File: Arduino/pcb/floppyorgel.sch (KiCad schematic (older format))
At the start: 2 parts, among them J1 VCC_Power_Select

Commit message: pcb: add switch for VCC power select
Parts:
- J1: footprint Connector_PinHeader_2.54mm:PinHeader_1x03_P2.54mm_Vertical -> w_switch:switch_mmp122-r
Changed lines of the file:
@@
 F 0 "J1" H 5672 2357 50  0000 R CNN
 F 1 "VCC_Power_Select" H 5672 2448 50  0000 R CNN
-F 2 "Connector_PinHeader_2.54mm:PinHeader_1x03_P2.54mm_Vertical" H 5700 2425 50  0001 C CNN
+F 2 "w_switch:switch_mmp122-r" H 5700 2425 50  0001 C CNN
 F 3 "~" H 5700 2425 50  0001 C CNN
 	1    5700 2425

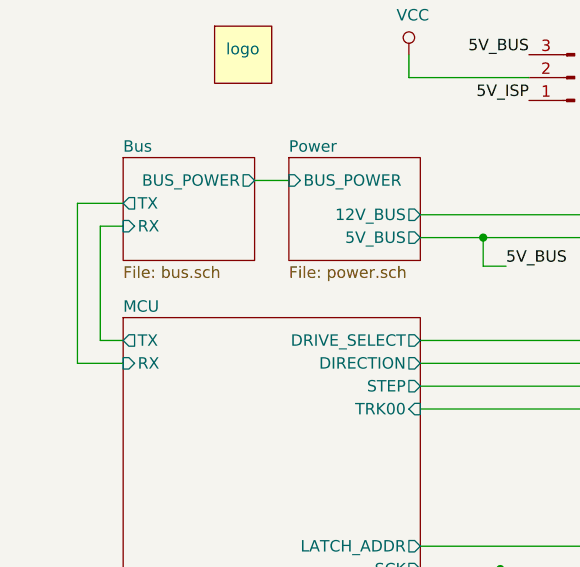
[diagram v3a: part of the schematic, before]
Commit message: pcb: mcu / bus: improve TX/RX labels for RS485 transceiver
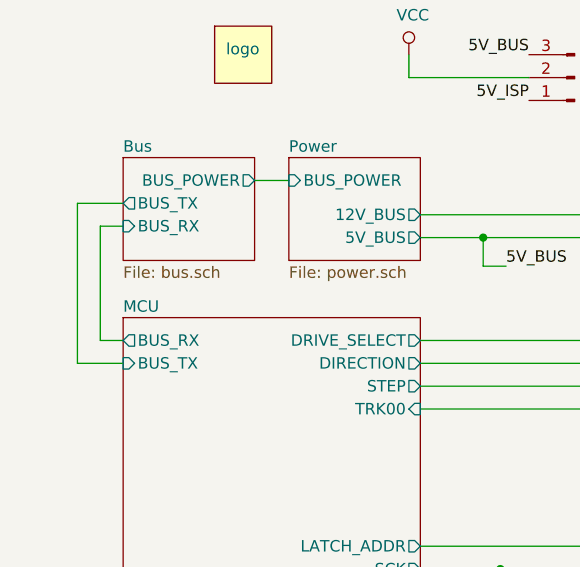
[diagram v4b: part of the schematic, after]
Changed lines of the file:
@@
 F1 "bus.sch" 50
 F2 "BUS_POWER" O R 4300 2875 50
-F3 "TX" O L 3725 2975 50
-F4 "RX" I L 3725 3075 50
+F3 "BUS_TX" O L 3725 2975 50
+F4 "BUS_RX" I L 3725 3075 50
 $EndSheet
 $Sheet
@@
 F10 "MISO" O L 5800 4675 50
 $EndSheet
-$Sheet
-S 3725 3475 1300 1950
-U 5CCFEC3E
-F0 "MCU" 50
-F1 "mcu.sch" 50
-F2 "DRIVE_SELECT" O R 5025 3575 50
-F3 "DIRECTION" O R 5025 3675 50
-F4 "STEP" O R 5025 3775 50
-F5 "MISO" I R 5025 4675 50
-F6 "SCK" O R 5025 4575 50
-F7 "TRK00" I R 5025 3875 50
-F8 "LATCH_ADDR" O R 5025 4475 50
-F9 "5V_ISP" O L 3725 5250 50
-F10 "RX" I L 3725 3675 50
-F11 "TX" O L 3725 3575 50
-F12 "LATCH_LED" O R 5025 5125 50
-F13 "MOSI" O R 5025 5225 50
-$EndSheet
 Text Label 5500 2325 2    50   ~ 0
 5V_BUS
@@
 	1    0    0    -1
 $EndComp
+$Sheet
+S 3725 3475 1300 1950
+U 5CCFEC3E
+F0 "MCU" 50
+F1 "mcu.sch" 50
+F2 "DRIVE_SELECT" O R 5025 3575 50
+F3 "DIRECTION" O R 5025 3675 50
+F4 "STEP" O R 5025 3775 50
+F5 "MISO" I R 5025 4675 50
+F6 "SCK" O R 5025 4575 50
+F7 "TRK00" I R 5025 3875 50
+F8 "LATCH_ADDR" O R 5025 4475 50
+F9 "5V_ISP" O L 3725 5250 50
+F10 "LATCH_LED" O R 5025 5125 50
+F11 "MOSI" O R 5025 5225 50
+F12 "BUS_TX" I L 3725 3675 50
+F13 "BUS_RX" O L 3725 3575 50
+$EndSheet
 $EndSCHEMATC

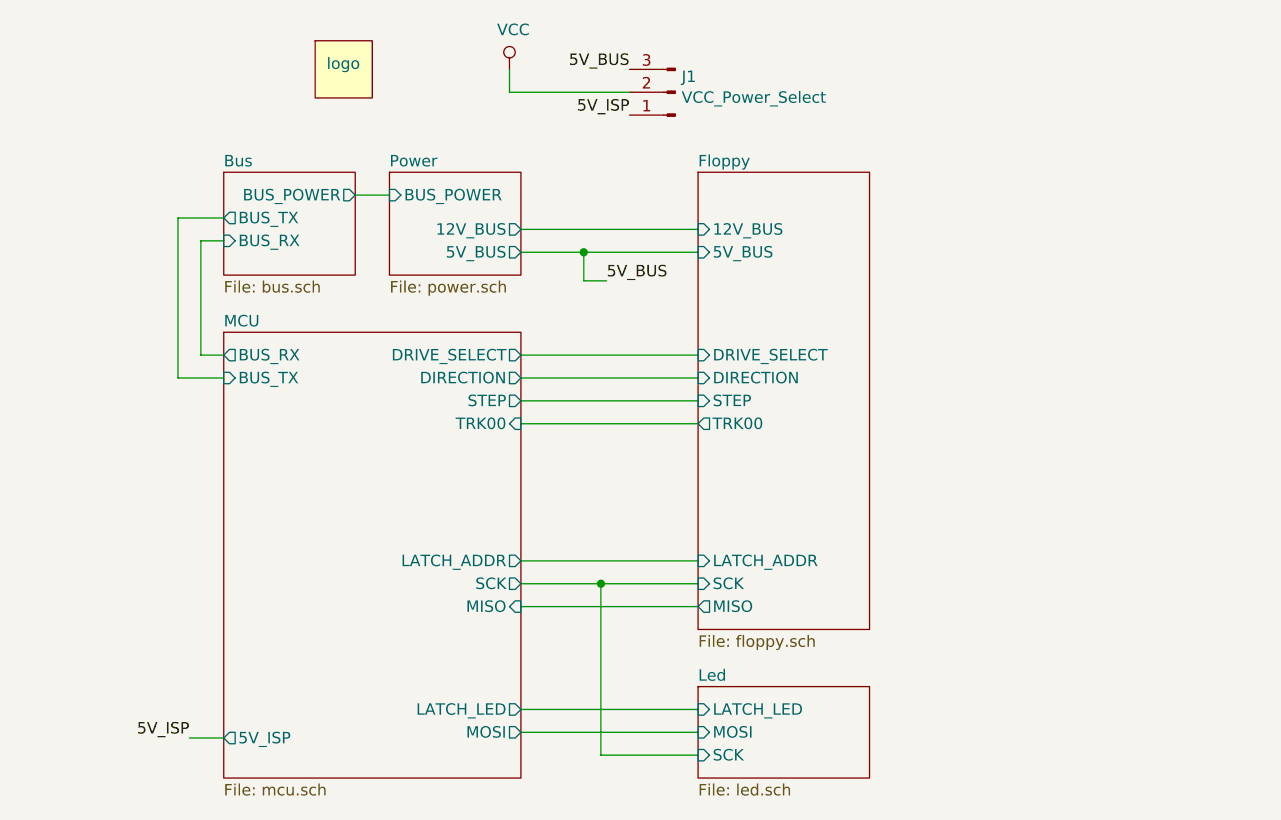
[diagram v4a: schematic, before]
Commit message: pcb / floppy: remove 4094 shift register / connect address connector directly
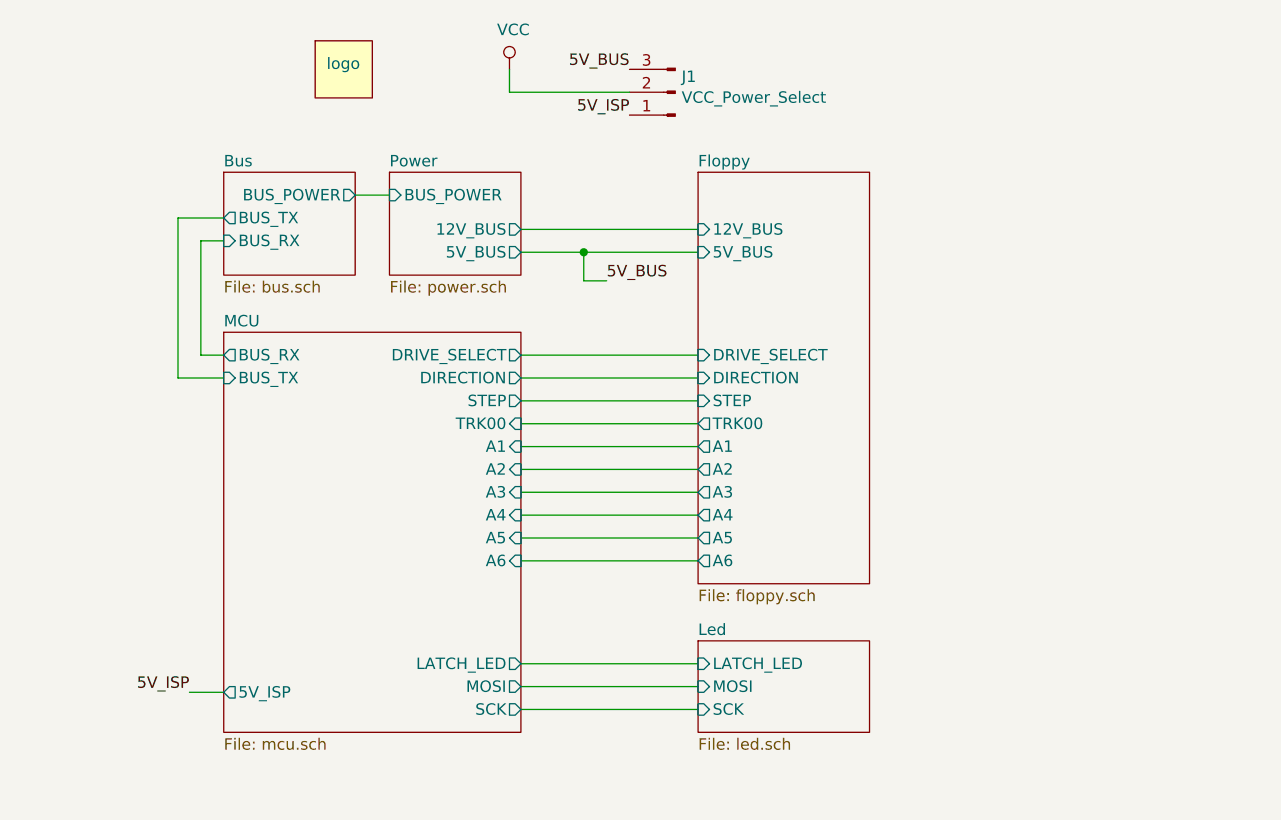
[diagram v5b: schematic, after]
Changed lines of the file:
@@
 Wire Wire Line
 	5800 3775 5025 3775
-$Comp
-L power:VCC #PWR01
-U 1 1 5D10B089
-P 4975 2325
-AR Path="/5D10B089" Ref="#PWR01"  Part="1"
-AR Path="/5CD31258/5D10B089" Ref="#PWR?"  Part="1"
-F 0 "#PWR01" H 4975 2175 50  0001 C CNN
-F 1 "VCC" H 4992 2498 50  0000 C CNN
-F 2 "" H 4975 2325 50  0001 C CNN
-F 3 "" H 4975 2325 50  0001 C CNN
-	1    4975 2325
-	1    0    0    -1
-$EndComp
-Wire Wire Line
-	4975 2325 4975 2425
-Wire Wire Line
-	4975 2425 5500 2425
-$Comp
-L vcc_power_select:VCC_Power_Select J1
-U 1 1 5D19C0BF
-P 5700 2425
-F 0 "J1" H 5672 2357 50  0000 R CNN
-F 1 "VCC_Power_Select" H 5672 2448 50  0000 R CNN
-F 2 "w_switch:switch_mmp122-r" H 5700 2425 50  0001 C CNN
-F 3 "~" H 5700 2425 50  0001 C CNN
-	1    5700 2425
-	-1   0    0    1
-$EndComp
-Wire Wire Line
-	5800 4675 5025 4675
-Wire Wire Line
-	5025 4475 5800 4475
 Wire Wire Line
 	3625 3575 3725 3575
@@
 Wire Wire Line
 	5025 3025 5800 3025
-Text Label 5500 2525 2    50   ~ 0
-5V_ISP
-Wire Wire Line
-	3575 5250 3725 5250
-Text Label 3575 5250 2    50   ~ 0
-5V_ISP
 Wire Wire Line
 	5025 3575 5800 3575
 Wire Wire Line
 	5025 3675 5800 3675
-$Sheet
-S 5800 2775 750  2000
-U 5CD0EE48
-F0 "Floppy" 50
-F1 "floppy.sch" 50
-F2 "DRIVE_SELECT" I L 5800 3575 50
-F3 "DIRECTION" I L 5800 3675 50
-F4 "TRK00" O L 5800 3875 50
-F5 "STEP" I L 5800 3775 50
-F6 "5V_BUS" I L 5800 3125 50
-F7 "12V_BUS" I L 5800 3025 50
-F8 "LATCH_ADDR" I L 5800 4475 50
-F9 "SCK" I L 5800 4575 50
-F10 "MISO" O L 5800 4675 50
-$EndSheet
-Text Label 5500 2325 2    50   ~ 0
-5V_BUS
 Wire Wire Line
 	5025 3125 5300 3125
@@
 	5300 3125 5800 3125
 $Sheet
-S 5800 5025 750  400
+S 5800 4825 750  400
 U 5CD3FBA6
 F0 "Led" 50
 F1 "led.sch" 50
-F2 "MOSI" I L 5800 5225 50
-F3 "SCK" I L 5800 5325 50
-F4 "LATCH_LED" I L 5800 5125 50
+F2 "MOSI" I L 5800 5025 50
+F3 "SCK" I L 5800 5125 50
+F4 "LATCH_LED" I L 5800 4925 50
 $EndSheet
 Wire Wire Line
-	5025 4575 5375 4575
+	5025 4275 5800 4275
 Wire Wire Line
-	5025 5125 5800 5125
-Connection ~ 5375 4575
+	5025 4375 5800 4375
 Wire Wire Line
-	5375 4575 5800 4575
+	5025 4475 5800 4475
 Wire Wire Line
-	5800 5325 5375 5325
+	5025 4175 5800 4175
 Wire Wire Line
-	5375 4575 5375 5325
+	5800 4075 5025 4075
 Wire Wire Line
-	5025 5225 5800 5225
+	5025 3975 5800 3975
 $Comp
 L logo:logo L1
@@
 	1    0    0    -1
 $EndComp
+Text Label 5500 2325 2    50   ~ 0
+5V_BUS
+Text Label 5500 2525 2    50   ~ 0
+5V_ISP
+$Comp
+L vcc_power_select:VCC_Power_Select J1
+U 1 1 5D19C0BF
+P 5700 2425
+F 0 "J1" H 5672 2357 50  0000 R CNN
+F 1 "VCC_Power_Select" H 5672 2448 50  0000 R CNN
+F 2 "w_switch:switch_mmp122-r" H 5700 2425 50  0001 C CNN
+F 3 "~" H 5700 2425 50  0001 C CNN
+	1    5700 2425
+	-1   0    0    1
+$EndComp
+Wire Wire Line
+	4975 2425 5500 2425
+Wire Wire Line
+	4975 2325 4975 2425
+$Comp
+L power:VCC #PWR01
+U 1 1 5D10B089
+P 4975 2325
+AR Path="/5D10B089" Ref="#PWR01"  Part="1"
+AR Path="/5CD31258/5D10B089" Ref="#PWR?"  Part="1"
+F 0 "#PWR01" H 4975 2175 50  0001 C CNN
+F 1 "VCC" H 4992 2498 50  0000 C CNN
+F 2 "" H 4975 2325 50  0001 C CNN
+F 3 "" H 4975 2325 50  0001 C CNN
+	1    4975 2325
+	1    0    0    -1
+$EndComp
 $Sheet
-S 3725 3475 1300 1950
+S 5800 2775 750  1800
+U 5CD0EE48
+F0 "Floppy" 50
+F1 "floppy.sch" 50
+F2 "DRIVE_SELECT" I L 5800 3575 50
+F3 "DIRECTION" I L 5800 3675 50
+F4 "TRK00" O L 5800 3875 50
+F5 "STEP" I L 5800 3775 50
+F6 "5V_BUS" I L 5800 3125 50
+F7 "12V_BUS" I L 5800 3025 50
+F8 "A4" O L 5800 4275 50
+F9 "A5" O L 5800 4375 50
+F10 "A6" O L 5800 4475 50
+F11 "A3" O L 5800 4175 50
+F12 "A2" O L 5800 4075 50
+F13 "A1" O L 5800 3975 50
+$EndSheet
+Wire Wire Line
+	5025 4925 5800 4925
+Wire Wire Line
+	5025 5025 5800 5025
+Wire Wire Line
+	5025 5125 5800 5125
+$Sheet
+S 3725 3475 1300 1750
 U 5CCFEC3E
 F0 "MCU" 50
@@
 F3 "DIRECTION" O R 5025 3675 50
 F4 "STEP" O R 5025 3775 50
-F5 "MISO" I R 5025 4675 50
-F6 "SCK" O R 5025 4575 50
-F7 "TRK00" I R 5025 3875 50
-F8 "LATCH_ADDR" O R 5025 4475 50
-F9 "5V_ISP" O L 3725 5250 50
-F10 "LATCH_LED" O R 5025 5125 50
-F11 "MOSI" O R 5025 5225 50
-F12 "BUS_TX" I L 3725 3675 50
-F13 "BUS_RX" O L 3725 3575 50
+F5 "SCK" O R 5025 5125 50
+F6 "TRK00" I R 5025 3875 50
+F7 "5V_ISP" O L 3725 5050 50
+F8 "LATCH_LED" O R 5025 4925 50
+F9 "MOSI" O R 5025 5025 50
+F10 "BUS_TX" I L 3725 3675 50
+F11 "BUS_RX" O L 3725 3575 50
+F12 "A1" I R 5025 3975 50
+F13 "A2" I R 5025 4075 50
+F14 "A3" I R 5025 4175 50
+F15 "A4" I R 5025 4275 50
+F16 "A5" I R 5025 4375 50
+F17 "A6" I R 5025 4475 50
 $EndSheet
+Text Label 3575 5050 2    50   ~ 0
+5V_ISP
+Wire Wire Line
+	3575 5050 3725 5050
 $EndSCHEMATC

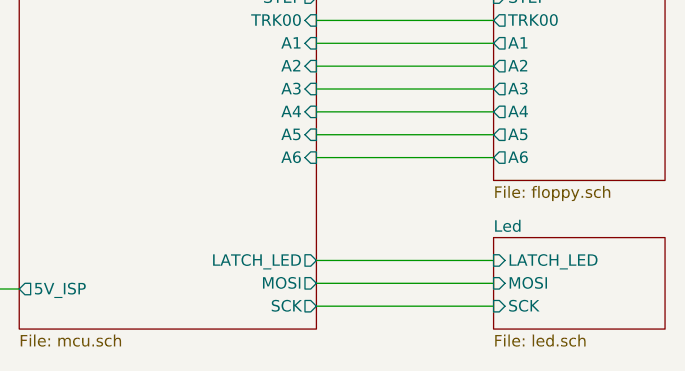
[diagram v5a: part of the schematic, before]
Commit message: pcb / led: remove hc595 shift register / connect led directly
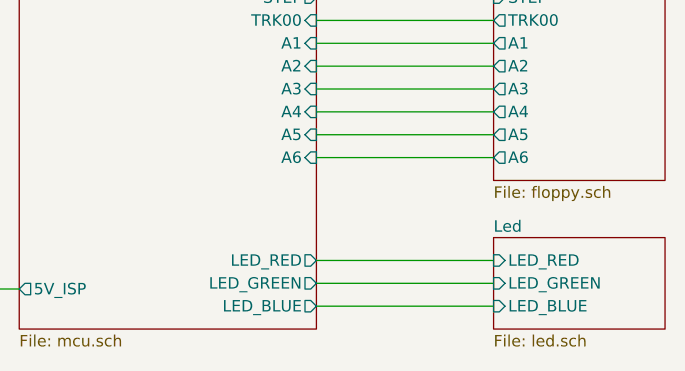
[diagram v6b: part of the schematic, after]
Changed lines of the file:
@@
 F0 "Led" 50
 F1 "led.sch" 50
-F2 "MOSI" I L 5800 5025 50
-F3 "SCK" I L 5800 5125 50
-F4 "LATCH_LED" I L 5800 4925 50
+F2 "LED_RED" I L 5800 4925 50
+F3 "LED_GREEN" I L 5800 5025 50
+F4 "LED_BLUE" I L 5800 5125 50
 $EndSheet
 Wire Wire Line
@@
 Wire Wire Line
 	5025 5125 5800 5125
+Text Label 3575 5050 2    50   ~ 0
+5V_ISP
+Wire Wire Line
+	3575 5050 3725 5050
 $Sheet
 S 3725 3475 1300 1750
@@
 F3 "DIRECTION" O R 5025 3675 50
 F4 "STEP" O R 5025 3775 50
-F5 "SCK" O R 5025 5125 50
-F6 "TRK00" I R 5025 3875 50
-F7 "5V_ISP" O L 3725 5050 50
-F8 "LATCH_LED" O R 5025 4925 50
-F9 "MOSI" O R 5025 5025 50
-F10 "BUS_TX" I L 3725 3675 50
-F11 "BUS_RX" O L 3725 3575 50
-F12 "A1" I R 5025 3975 50
-F13 "A2" I R 5025 4075 50
-F14 "A3" I R 5025 4175 50
-F15 "A4" I R 5025 4275 50
-F16 "A5" I R 5025 4375 50
-F17 "A6" I R 5025 4475 50
+F5 "TRK00" I R 5025 3875 50
+F6 "5V_ISP" O L 3725 5050 50
+F7 "BUS_TX" I L 3725 3675 50
+F8 "BUS_RX" O L 3725 3575 50
+F9 "A1" I R 5025 3975 50
+F10 "A2" I R 5025 4075 50
+F11 "A3" I R 5025 4175 50
+F12 "A4" I R 5025 4275 50
+F13 "A5" I R 5025 4375 50
+F14 "A6" I R 5025 4475 50
+F15 "LED_RED" O R 5025 4925 50
+F16 "LED_GREEN" O R 5025 5025 50
+F17 "LED_BLUE" O R 5025 5125 50
 $EndSheet
-Text Label 3575 5050 2    50   ~ 0
-5V_ISP
-Wire Wire Line
-	3575 5050 3725 5050
 $EndSCHEMATC
